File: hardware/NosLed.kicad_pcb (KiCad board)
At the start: 2 copper layers, 37 x 100 mm, 56 parts, among them J101 AC, J102 USB_C_Receptacle_USB2.0_16P, J103 LOAD, U101 AMS1117-3.3, U102 ESP32-C3-WROOM-02U, U301 BP2876, U401 LNK306D, U501 BP2876

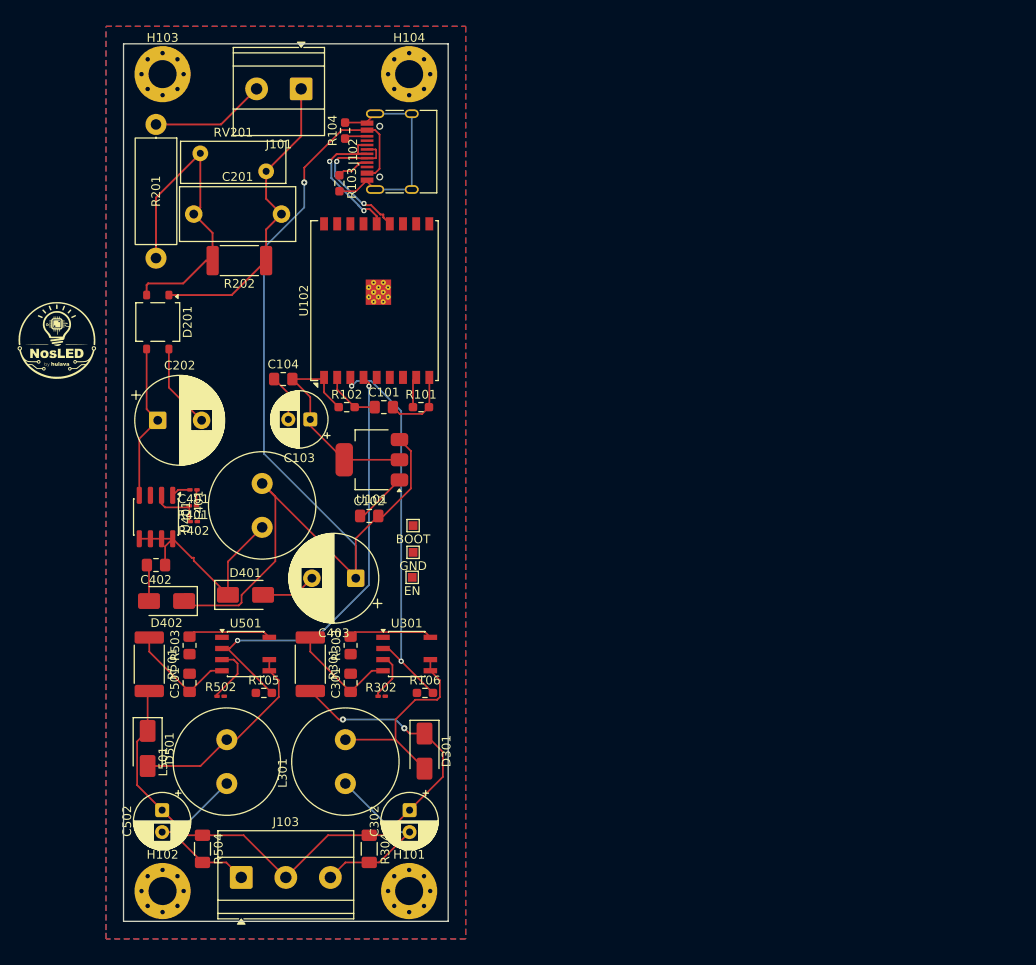
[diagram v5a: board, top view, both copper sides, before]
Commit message: Tracing 0.2
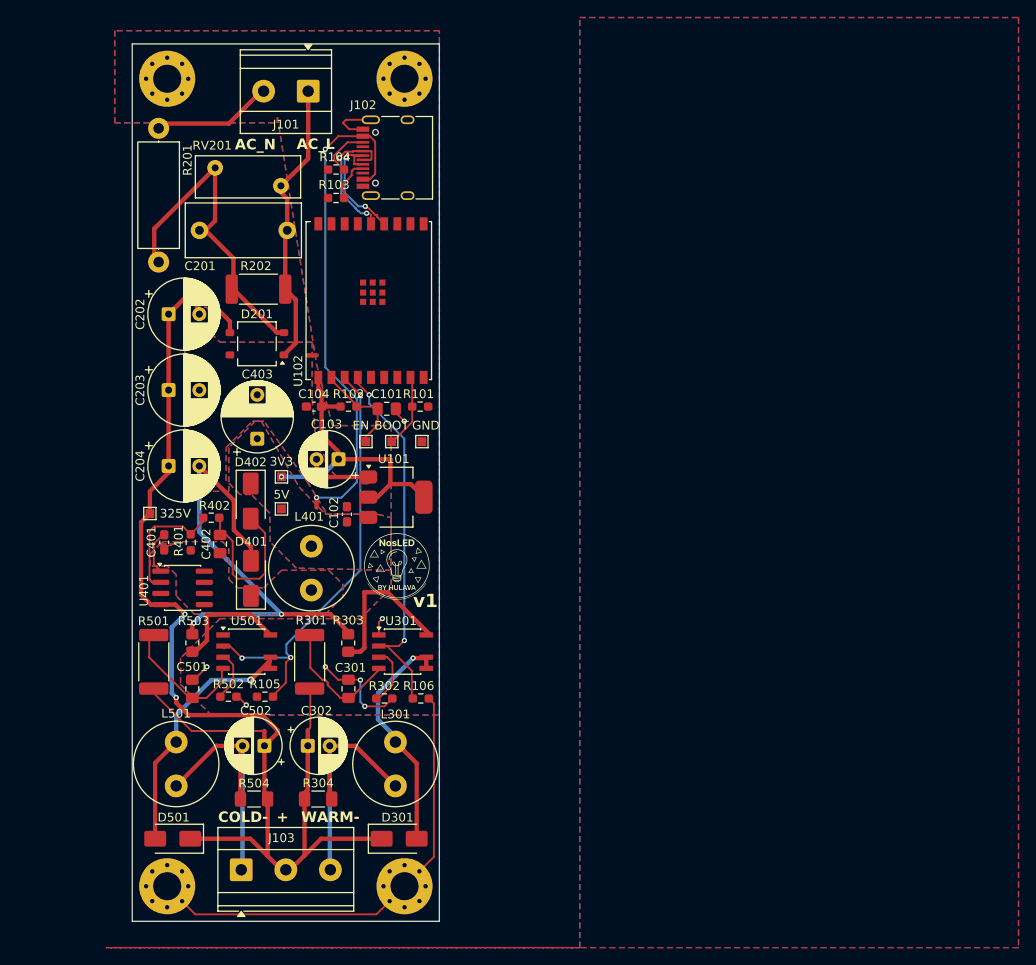
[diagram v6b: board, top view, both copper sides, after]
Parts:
- added C203: 8.2uF 400v, Capacitor_THT:CP_Radial_D8.0mm_P3.50mm, F.Cu at (35.1, 78.5)
- added C204: 8.2uF 400v, Capacitor_THT:CP_Radial_D8.0mm_P3.50mm, F.Cu at (35.1, 87.1)
- added NT101: NetTie_2, NetTie:NetTie-2_SMD_Pad0.5mm, F.Cu at (52.0, 91.4)
- added NT102: NetTie_2, NetTie:NetTie-2_SMD_Pad0.5mm, F.Cu at (51.5, 74.5)
- added NT302: NetTie_2, NetTie:NetTie-2_SMD_Pad0.5mm, F.Cu at (51.0, 117.7)
- added NT502: NetTie_2, NetTie:NetTie-2_SMD_Pad0.5mm, F.Cu at (46.1, 117.8)
- added TP_104: 5V, NosLib:TestPoint_Pad_1.0x1.0mm, F.Cu at (48.0, 92.0)
- added TP_105: 3V3, NosLib:TestPoint_Pad_1.0x1.0mm, F.Cu at (48.0, 88.3)
- added TP_106: 325V, NosLib:TestPoint_Pad_1.0x1.0mm, F.Cu at (33.0, 92.5)
- C102, C104: footprint Capacitor_SMD:C_0805_2012Metric_Pad1.18x1.45mm_HandSolder -> Capacitor_SMD:C_0603_1608Metric_Pad1.08x0.95mm_HandSolder
- C202: value 22uF 400v -> 8.2uF 400v; footprint Capacitor_THT:CP_Radial_D10.0mm_P5.00mm -> Capacitor_THT:CP_Radial_D8.0mm_P3.50mm
- C401: footprint Capacitor_SMD:C_0201_0603Metric_Pad0.64x0.40mm_HandSolder -> Capacitor_SMD:C_0603_1608Metric_Pad1.08x0.95mm_HandSolder
- C403: footprint Capacitor_THT:CP_Radial_D10.0mm_P5.00mm -> Capacitor_THT:CP_Radial_D8.0mm_P5.00mm
- J101: footprint TerminalBlock_Phoenix:TerminalBlock_Phoenix_MKDS-1,5-2-5.08_1x02_P5.08mm_Horizontal -> NosLib:TerminalBlock_Phoenix_MKDS-1,5-2-5.08_1x02_P5.08mm_Horizontal
- J103: footprint TerminalBlock_Phoenix:TerminalBlock_Phoenix_MKDS-1,5-3-5.08_1x03_P5.08mm_Horizontal -> NosLib:TerminalBlock_Phoenix_MKDS-1,5-3-5.08_1x03_P5.08mm_Horizontal
- L301, L401, L501: footprint Inductor_THT:L_Radial_D12.0mm_P5.00mm_Neosid_SD12k_style2 -> Inductor_THT:L_Radial_D9.5mm_P5.00mm_Fastron_07HVP
- R302, R401, R402, R502: footprint Resistor_SMD:R_0201_0603Metric_Pad0.64x0.40mm_HandSolder -> Resistor_SMD:R_0603_1608Metric_Pad0.98x0.95mm_HandSolder
- U102: footprint RF_Module:ESP32-C3-WROOM-02U -> PCM_Espressif:ESP32-C3-WROOM-02U
- moved G*** 46.3 mm to (61.2, 98.5)
- moved C403 19.5 mm to (45.2, 84.0), turned to 90 degrees
- moved TP_103 16.3 mm to (57.6, 84.3)
- moved D402 14.9 mm to (44.5, 91.1), turned to -90 degrees
- moved C502 13.8 mm to (46.1, 119.0), turned to 180 degrees
- moved C302 13.7 mm to (51.0, 119.0), turned to 0 degrees
- moved TP_102 12.7 mm to (64.0, 84.3)
- moved C202 12.2 mm to (35.1, 69.8)
- moved D201 11.6 mm to (45.2, 73.2), turned to 180 degrees
- moved D501 10.7 mm to (35.6, 129.6), turned to 180 degrees
- moved D301 10.4 mm to (61.4, 129.6), turned to 0 degrees
- moved TP_101 9.87 mm to (60.6, 84.3)
- moved L401 9.08 mm to (51.4, 101.2)
- moved U401 8.62 mm to (36.7, 101.0), turned to 0 degrees
- moved R504 8.17 mm to (44.9, 125.1), turned to 180 degrees
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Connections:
- net Net-(D401-K) renamed /LNK302PN/SOURCE
- C102 pad 1: GND -> PWR_GND
- C103 pad 2: GND -> PWR_GND
- C104 pad 1: GND -> PWR_GND
- C202 pad 1: /ACInput/325V -> /325V
- C202 pad 2: GND -> PWR_GND
- C302 pad 1: /ACInput/325V -> /325V
- C403 pad 2: GND -> PWR_GND
- C502 pad 1: /ACInput/325V -> /325V
- D201 pad 3: /ACInput/325V -> /325V
- D201 pad 4: GND -> PWR_GND
- D301 pad 1: /ACInput/325V -> /325V
- D401 pad 2: GND -> PWR_GND
- D501 pad 1: /ACInput/325V -> /325V
- J102 pad A4: 5V -> Net-(J102-VBUS-PadA4)
- J102 pad A9: 5V -> Net-(J102-VBUS-PadA4)
- J102 pad B4: 5V -> Net-(J102-VBUS-PadA4)
- J102 pad B9: 5V -> Net-(J102-VBUS-PadA4)
- J103 pad 2: /ACInput/325V -> /325V
- R301 pad 2: /ACInput/325V -> Net-(NT302-Pad1)
- R303 pad 1: GND -> PWR_GND
- R304 pad 1: /ACInput/325V -> /325V
- R501 pad 2: /ACInput/325V -> Net-(NT502-Pad1)
- R503 pad 1: GND -> PWR_GND
- R504 pad 1: /ACInput/325V -> /325V
- U101 pad 1: GND -> PWR_GND
- U102 pad 3: PWM_WARM -> PWM_COLD
- U102 pad 4: PWM_COLD -> PWM_WARM
- U401 pad 4: /ACInput/325V -> /325V
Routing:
- net /325V: track 0.00 -> 127.2 mm, vias 0 -> 2
- net 5V: track 127.1 -> 0.00 mm, vias 1 -> 0
- net /ACInput/325V: track 94.4 -> 0.00 mm, vias 2 -> 0
- net PWR_GND: track 0.00 -> 62.6 mm, vias 0 -> 2
- net Net-(J102-VBUS-PadA4): track 0.00 -> 56.6 mm, vias 0 -> 2
- net /LNK302PN/SOURCE: track 27.5 -> 0.00 mm
- net GND: track 61.7 -> 77.6 mm, vias 0 -> 7
- net Net-(NT502-Pad1): track 0.00 -> 15.1 mm
- net Net-(D402-A): track 4.20 -> 18.6 mm
- net 3V3: track 25.7 -> 35.6 mm, vias 0 -> 1
- net /BP2876D_COLD/LOAD-: track 20.8 -> 30.3 mm
- net /BP2876D_WARM/LOAD-: track 20.8 -> 30.2 mm
- net Net-(U401-FB): track 6.21 -> 14.7 mm
- net /BP2876D_WARM/CS: track 9.55 -> 17.6 mm
- net /BP2876D_COLD/DRAIN: track 22.9 -> 30.0 mm, vias 0 -> 1
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- added copper zone on B.Cu, net /LNK302PN/SOURCE
- added copper zone on F.Cu, net /LNK302PN/SOURCE
- added copper zone on B.Cu, net 5V
- added copper zone on F.Cu, net 5V
- added copper zone on B.Cu, net PWR_GND
- added copper zone on F.Cu, net PWR_GND
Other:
- board size 37 x 100 mm -> 35 x 100 mm
- board text added: "+"
- board text added: "AC_L"
- board text added: "AC_N"
- board text added: "COLD-"
- board text added: "WARM-"
- board text added: "v1"

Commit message: Version 1
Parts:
- moved R103 14.9 mm to (56.2, 41.8)
- moved NT502 14.1 mm to (32.9, 112.8), turned to 180 degrees
- moved R104 8.17 mm to (56.2, 45.4)
- moved R106 7.45 mm to (63.8, 106.2)
- moved R302 7.45 mm to (59.6, 106.2)
- moved R502 7.29 mm to (42.7, 106.2)
- moved R105 7.29 mm to (46.9, 106.2)
- moved NT302 4.80 mm to (46.2, 117.5), turned to -135 degrees
- moved U501 3.51 mm to (44.8, 111.7)
- moved U301 3.42 mm to (61.8, 111.7)
- moved NT101 2.94 mm to (49.1, 91.0), turned to -135 degrees
- moved R501 1.32 mm to (34.8, 109.4)
- moved C401 1.09 mm to (33.6, 96.0)
- moved C501 1.09 mm to (38.9, 112.5)
- moved R503 1.06 mm to (38.9, 107.3)
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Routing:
- net GND: track 77.6 -> 35.1 mm, vias 7 -> 4
- net 5V: track 0.00 -> 25.2 mm
- net /325V: track 127.2 -> 143.0 mm
- net Net-(NT502-Pad1): track 15.1 -> 0.00 mm
- net Net-(D402-A): track 18.6 -> 5.61 mm
- net Net-(J102-CC1): track 4.92 -> 14.6 mm, vias 0 -> 2
- net /BP2876D_WARM/CS: track 17.6 -> 9.25 mm
- net /LNK302PN/SOURCE: track 0.00 -> 7.20 mm
- net /BP2876D_WARM/DRAIN: track 26.9 -> 19.7 mm, vias 1 -> 0
- net /BP2876D_COLD/LOAD-: track 30.3 -> 23.7 mm
- net /BP2876D_WARM/LOAD-: track 30.2 -> 23.7 mm
- net PWM_COLD: track 50.4 -> 45.9 mm, vias 3 -> 2
- net /BP2876D_COLD/CS: track 13.4 -> 9.25 mm
- net USB_D+: track 15.5 -> 12.2 mm, vias 2 -> 0
- net USB_D-: track 15.3 -> 12.1 mm, vias 2 -> 0
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- removed copper zone on B.Cu, net 5V
- removed copper zone on F.Cu, net 5V
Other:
- outline, holes or cut-outs redrawn

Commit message: Fixes
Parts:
- renumbered C102 to C101, C103 to C102, C104 to C103, C101 to C104, C302 to C301, C301 to C302, C402 to C401, C401 to C402, C502 to C501, C501 to C502, D402 to D401, D401 to D402, J102 to J101, J103 to J102, J101 to J103, NT102 to NT101, NT101 to NT102, NT302 to NT301, NT502 to NT501, R304 to R301, R301 to R302, R302 to R303, R303 to R304, R402 to R401, R401 to R402, R504 to R501, R501 to R502, R502 to R503, R503 to R504, TP_104 to TP_101, TP_105 to TP_102, TP_101 to TP_103, TP_103 to TP_104, TP_102 to TP_105
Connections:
- R101 pad 2: GND -> 3V3
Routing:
- net 3V3: track 36.8 -> 47.7 mm, vias 1 -> 3
- net GND: track 35.1 -> 40.7 mm, vias 4 -> 6
